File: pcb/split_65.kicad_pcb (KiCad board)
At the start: 2 copper layers, 373.9 x 95.3 mm, 312 parts, among them J1 PJ-3200B-4A, J10 AVR-ISP-6, J11 Breakaway_Tabs, J12 Breakaway_Tabs, J13 Breakaway_Tabs, J14 Breakaway_Tabs, J15 Breakaway_Tabs, J16 Breakaway_Tabs, J2 AVR-ISP-6, J3 Breakaway_Tabs, J4 Breakaway_Tabs, J5 Breakaway_Tabs, J6 Breakaway_Tabs, J7 Breakaway_Tabs, J8 Breakaway_Tabs, J9 PJ-3200B-4A, Q1 2N7002, Q2 2N7002, SW1 SW_Push, SW2 SW_Push, U1 ATmega32U4-AU, U2 PRTR5V0U2X, U3 ATmega32U4-AU, U4 PRTR5V0U2X, Y1 16MHz, Y2 16MHz

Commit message: laid out diodes and resistors
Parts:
- removed MH1, MH2: HOLE, MountingHole:MountingHole_5mm
- C1, C10, C11, C12, C13, C14, C2, C3, C4, C5, C6, C7, C8, C9, D1, D10, D11, D12, D13, D14, D15, D16, D17, D18, D19, D2, D20, D21, D22, D23, D24, D25, D26, D27, D28, D29, D3, D30, D31, D32, D33, D34, D35, D36, D37, D38, D39, D4, D40, D41, D42, D43, D44, D45, D46, D47, D48, D49, D5, D50, D51, D52, D53, D54, D55, D56, D57, D58, D59, D6, D60, D61, D62, D63, D64, D65, D66, D67, D68, D69, D7, D70, D71, D72, D73, D74, D75, D76, D77, D78, D79, D8, D80, D81, D82, D9, F1, F2, FID1, FID2, FID3, FID4, FID5, FID6, J10, J11, J12, J13, J14, J15, J16, J2, J3, J4, J5, J6, J7, J8, Q1, Q2, R1, R10, R11, R12, R13, R14, R15, R16, R17, R18, R19, R2, R20, R21, R22, R23, R24, R25, R26, R27, R28, R29, R3, R30, R31, R32, R33, R34, R35, R36, R37, R38, R39, R4, R40, R41, R42, R43, R44, R45, R46, R47, R48, R49, R5, R50, R51, R52, R53, R54, R55, R56, R57, R58, R59, R6, R60, R61, R62, R63, R64, R65, R66, R67, R68, R69, R7, R70, R71, R72, R73, R74, R75, R76, R77, R78, R79, R8, R80, R81, R82, R83, R84, R85, R86, R87, R88, R89, R9, R90, R91, R92, R93, R94, R95, R96, SW1, SW2, U1, U2, U3, U4, Y1, Y2: moved to B.Cu
- moved D8 336.0 mm to (35.7, 81.0), turned to 90 degrees
- moved D22 329.4 mm to (35.7, 119.1), turned to 90 degrees
- moved R17 323.3 mm to (35.7, 104.8), turned to 270 degrees
- moved R11 315.6 mm to (64.3, 85.7), turned to 270 degrees
- moved D9 313.6 mm to (64.4, 81.0), turned to 90 degrees
- moved R2 311.9 mm to (78.6, 66.7), turned to 270 degrees
- moved D46 311.2 mm to (381.0, 61.9), turned to 90 degrees
- moved R32 302.1 mm to (35.7, 142.9), turned to 270 degrees
- moved R88 297.9 mm to (60.3, 190.0), turned to 180 degrees
- moved Q1 297.7 mm to (60.4, 166.1), turned to 180 degrees
- moved Q2 297.7 mm to (60.4, 169.7), turned to 180 degrees
- moved R44 296.9 mm to (60.8, 201.7), turned to 180 degrees
- moved J9 294.0 mm to (264.3, 39.0), turned to 270 degrees
- moved D10 290.9 mm to (88.1, 81.0), turned to 90 degrees
- moved R91 290.1 mm to (64.2, 202.9), turned to 180 degrees
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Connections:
- MX33 pad 1: COL2 -> COL3
- MX33 pad 2: Net-(D31-Pad2) -> Net-(D32-Pad2)
- MX34 pad 4: Net-(MX33-Pad4) -> Net-(MX34-Pad4)
- MX35 pad 4: Net-(MX35-Pad4) -> Net-(MX33-Pad4)
- R34 pad 2: Net-(MX33-Pad4) -> Net-(MX34-Pad4)
- R35 pad 2: Net-(MX35-Pad4) -> Net-(MX33-Pad4)
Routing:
- net LEDGND: track 0.00 -> 455.2 mm
- net +5V: track 0.00 -> 136.0 mm
- net ROW2: track 0.00 -> 124.7 mm
- net ROW1: track 0.00 -> 119.9 mm
- net ROW4: track 0.00 -> 115.5 mm
- net ROW0: track 0.00 -> 105.7 mm
- net COL5: track 0.00 -> 69.7 mm
- net COL6: track 0.00 -> 69.6 mm
- net Net-(MX33-Pad4): track 0.00 -> 15.4 mm
- net Net-(MX31-Pad4): track 0.00 -> 9.77 mm
- net Net-(MX7-Pad4): track 0.00 -> 9.76 mm
- net Net-(MX14-Pad4): track 0.00 -> 9.76 mm
- net Net-(MX36-Pad4): track 0.00 -> 9.62 mm
- net Net-(MX12-Pad4): track 0.00 -> 7.16 mm
- net Net-(MX2-Pad4): track 0.00 -> 7.14 mm
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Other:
- board outline removed

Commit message: did edge cuts
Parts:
- J1, J9, USB1, USB2: moved to B.Cu
- moved D37 256.3 mm to (63.1, 75.6), turned to 90 degrees
- moved R42 209.6 mm to (60.7, 58.3), turned to 90 degrees
- moved R45 188.9 mm to (57.7, 56.9), turned to 270 degrees
- moved R41 172.0 mm to (63.1, 58.3), turned to 90 degrees
- moved U2 171.4 mm to (61.9, 54.2), turned to 270 degrees
- moved R44 145.9 mm to (68.1, 56.0)
- moved F1 144.2 mm to (63.1, 71.1), turned to 90 degrees
- moved D1 14.3 mm to (45.2, 61.9)
- moved R1 14.3 mm to (45.2, 66.7)
- moved J1 4.17 mm to (138.1, 44.6)
- moved USB1 2.38 mm to (61.9, 42.9), turned to 0 degrees
- turned U1 to 270 degrees
- turned USB2 to 0 degrees
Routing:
- net +5V: track 136.0 -> 332.0 mm
- net COL4: track 0.00 -> 93.0 mm
- net LEDGND: track 455.2 -> 533.5 mm
- net COL3: track 0.00 -> 69.7 mm
- net ROW3: track 0.00 -> 65.6 mm
- net GND: track 0.00 -> 62.4 mm
- net COL0: track 0.00 -> 59.5 mm
- net ROW0: track 105.7 -> 119.9 mm
- net Net-(MX16-Pad4): track 0.00 -> 12.0 mm
- net Net-(R41-Pad2): track 0.00 -> 11.2 mm
- net Net-(R42-Pad2): track 0.00 -> 10.6 mm
- net Net-(MX29-Pad4): track 0.00 -> 9.76 mm
- net Net-(MX22-Pad4): track 0.00 -> 9.76 mm
- net Net-(MX26-Pad4): track 0.00 -> 7.20 mm
- net Net-(MX28-Pad4): track 0.00 -> 7.16 mm
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- added copper zone on B.Cu, net GND
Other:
- board outline added: 158.4 x 105.4 mm

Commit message: edge cuts, route usb
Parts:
- moved R9 243.1 mm to (139.9, 60.5), turned to 90 degrees
- moved C7 205.8 mm to (57.2, 116.7)
- moved C5 201.0 mm to (45.2, 131.0)
- moved C4 199.9 mm to (40.5, 131.0)
- moved C6 197.6 mm to (57.2, 122.6)
- moved R8 146.1 mm to (136.3, 60.5), turned to 90 degrees
- moved R24 125.4 mm to (48.8, 108.3)
- moved Y1 80.0 mm to (58.3, 127.4)
- moved D5 14.3 mm to (121.4, 61.9)
- moved R5 14.3 mm to (121.4, 66.7)
- moved D37 13.8 mm to (50.1, 70.9), turned to 0 degrees
- moved F1 7.95 mm to (55.2, 70.9), turned to 0 degrees
- moved J9 5.62 mm to (264.3, 44.6)
- moved USB2 2.38 mm to (340.5, 42.9)
- moved R44 1.44 mm to (66.7, 56.0), turned to 0 degrees
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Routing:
- net GND: track 62.4 -> 149.2 mm
- net D+: track 0.00 -> 70.2 mm
- net D-: track 0.00 -> 70.2 mm
- net ROW0: track 119.9 -> 80.3 mm, vias 0 -> 2
- net LEDGND: track 533.5 -> 494.5 mm, vias 0 -> 6
- net +5V: track 332.0 -> 369.3 mm
- net VCC: track 0.00 -> 34.7 mm, vias 0 -> 2
- net Net-(R44-Pad1): track 0.00 -> 10.0 mm, vias 0 -> 2
- net Net-(MX5-Pad4): track 7.11 -> 0.00 mm
- net Net-(R45-Pad1): track 0.00 -> 6.26 mm, vias 0 -> 2
- net VBUS: track 0.00 -> 1.96 mm
- net ROW2: track 124.7 -> 125.1 mm, vias 0 -> 2
- net ROW1: track 119.9 -> 120.3 mm, vias 0 -> 2
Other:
- board size 158.4 x 105.4 mm -> 375 x 105.4 mm

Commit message: add switch, edit models
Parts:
- removed D77, D78: SOD-123, Diode_SMD:D_SOD-123
- removed D79, D80, D81: LED_3mm, locallib:LED_D3.0mm
- removed D82: Schottky, Diode_SMD:D_SOD-123
- removed R91: 1k, Resistor_SMD:R_0805_2012Metric
- removed R92, R93: 22, Resistor_SMD:R_0805_2012Metric
- removed R94: 10k, Resistor_SMD:R_0805_2012Metric
- removed R95, R96: 5.1k, Resistor_SMD:R_0805_2012Metric
- added D0: SOD-123, Diode_SMD:D_SOD-123, B.Cu at (35.7, 61.9)
- added MX0: MXOnly-1U, MX_Alps_Hybrid:MXOnly-1U, F.Cu at (28.6, 61.9)
- added R0: 470, Resistor_SMD:R_0805_2012Metric, B.Cu at (35.7, 66.7)
- D34: value LED_3mm -> Schottky; footprint locallib:LED_D3.0mm -> Diode_SMD:D_SOD-123
- D35, D36: value LED_3mm -> SOD-123; footprint locallib:LED_D3.0mm -> Diode_SMD:D_SOD-123
- D37: value Schottky -> SOD-123
- D76: value SOD-123 -> Schottky
- MX33: footprint MX_Alps_Hybrid:MXOnly-1.5U -> MX_Alps_Hybrid:MXOnly-1.25U
- MX34: footprint MX_Alps_Hybrid:MXOnly-1.25U -> MX_Alps_Hybrid:MXOnly-1.5U
- R38, R39: value 1k -> 22
- R40, R88: value 1k -> 10k
- R41, R42: value 22 -> 5.1k
- R43, R72: value 10k -> 470
- R44, R45: value 5.1k -> 470
- R69: value 470 -> 10k
- R85: value 470 -> 1k
- R86, R87: value 470 -> 22
- R89, R90: value 1k -> 5.1k
- moved D39 14.3 mm to (247.7, 61.9)
- moved R47 14.3 mm to (247.7, 66.7)
- moved R51 14.3 mm to (323.9, 66.7)
- moved D43 14.3 mm to (323.9, 61.9)
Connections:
- D34 pad 1: GND -> +5V
- D34 pad 2: Net-(D34-Pad2) -> VBUS
- D35 pad 1: GND -> ROW0-R
- D36 pad 1: GND -> ROW0-R
- D37 pad 1: +5V -> ROW0-R
- D37 pad 2: VBUS -> Net-(D37-Pad2)
- D44 pad 1: ROW0-R -> ROW1-R
- D45 pad 1: ROW0-R -> ROW1-R
- D46 pad 1: ROW0-R -> ROW1-R
- D53 pad 1: ROW1-R -> ROW2-R
- D54 pad 1: ROW1-R -> ROW2-R
- D55 pad 1: ROW1-R -> ROW2-R
- D61 pad 1: ROW2-R -> ROW3-R
- D62 pad 1: ROW2-R -> ROW3-R
- D63 pad 1: ROW2-R -> ROW3-R
- D69 pad 1: ROW3-R -> ROW4-R
- D70 pad 1: ROW3-R -> ROW4-R
- D71 pad 1: ROW3-R -> ROW4-R
- D76 pad 1: ROW4-R -> +5VA
- D76 pad 2: Net-(D76-Pad2) -> VDC
- MX1 pad 1: COL0 -> COL1
- MX10 pad 1: COL2 -> COL3
- MX11 pad 1: COL3 -> COL4
- MX12 pad 1: COL4 -> COL5
- MX13 pad 1: COL5 -> COL6
- MX14 pad 1: COL6 -> COL7
- MX15 pad 1: COL0 -> Net-(MX15-Pad1)
- MX18 pad 1: COL2 -> COL3
- MX19 pad 1: COL3 -> COL4
- MX2 pad 1: COL1 -> COL2
- MX20 pad 1: COL4 -> COL5
- MX21 pad 1: COL5 -> COL6
- MX22 pad 1: COL6 -> COL7
- MX23 pad 1: COL0 -> Net-(MX15-Pad1)
- MX25 pad 1: COL2 -> COL3
- MX26 pad 1: COL3 -> COL4
- MX27 pad 1: COL4 -> COL5
- MX28 pad 1: COL5 -> COL6
- MX29 pad 1: COL6 -> COL7
- MX3 pad 1: COL2 -> COL3
- MX30 pad 1: COL0 -> Net-(MX15-Pad1)
- MX33 pad 2: Net-(D32-Pad2) -> Net-(D31-Pad2)
- MX34 pad 1: COL2 -> COL4
- MX34 pad 2: Net-(D31-Pad2) -> Net-(D32-Pad2)
- MX35 pad 1: COL3 -> COL4
- MX35 pad 4: Net-(MX33-Pad4) -> Net-(MX34-Pad4)
- MX36 pad 1: COL4 -> COL5
- MX37 pad 1: COL4 -> COL5
- MX38 pad 2: Net-(D38-Pad2) -> Net-(D35-Pad2)
- MX39 pad 2: Net-(D39-Pad2) -> Net-(D36-Pad2)
- MX4 pad 1: COL3 -> COL4
- MX40 pad 2: Net-(D40-Pad2) -> Net-(D37-Pad2)
- MX41 pad 2: Net-(D41-Pad2) -> Net-(D38-Pad2)
- MX42 pad 2: Net-(D42-Pad2) -> Net-(D39-Pad2)
- MX43 pad 2: Net-(D43-Pad2) -> Net-(D40-Pad2)
- MX44 pad 2: Net-(D44-Pad2) -> Net-(D41-Pad2)
- MX45 pad 2: Net-(D45-Pad2) -> Net-(D42-Pad2)
- MX46 pad 2: Net-(D45-Pad2) -> Net-(D42-Pad2)
- MX47 pad 2: Net-(D46-Pad2) -> Net-(D43-Pad2)
- MX48 pad 2: Net-(D47-Pad2) -> Net-(D44-Pad2)
- MX49 pad 2: Net-(D48-Pad2) -> Net-(D45-Pad2)
- MX5 pad 1: COL4 -> COL5
- MX50 pad 2: Net-(D49-Pad2) -> Net-(D46-Pad2)
- MX51 pad 2: Net-(D50-Pad2) -> Net-(D47-Pad2)
- MX52 pad 2: Net-(D51-Pad2) -> Net-(D48-Pad2)
- MX53 pad 2: Net-(D52-Pad2) -> Net-(D49-Pad2)
- MX54 pad 2: Net-(D53-Pad2) -> Net-(D50-Pad2)
- MX55 pad 2: Net-(D54-Pad2) -> Net-(D51-Pad2)
- MX56 pad 2: Net-(D55-Pad2) -> Net-(D52-Pad2)
- MX57 pad 2: Net-(D56-Pad2) -> Net-(D53-Pad2)
- MX58 pad 2: Net-(D57-Pad2) -> Net-(D54-Pad2)
- MX59 pad 2: Net-(D58-Pad2) -> Net-(D55-Pad2)
- MX6 pad 1: COL5 -> COL6
- MX60 pad 2: Net-(D59-Pad2) -> Net-(D56-Pad2)
- MX61 pad 2: Net-(D60-Pad2) -> Net-(D57-Pad2)
- MX62 pad 2: Net-(D61-Pad2) -> Net-(D58-Pad2)
- MX63 pad 2: Net-(D62-Pad2) -> Net-(D59-Pad2)
- MX64 pad 2: Net-(D63-Pad2) -> Net-(D60-Pad2)
- MX65 pad 2: Net-(D64-Pad2) -> Net-(D61-Pad2)
- MX66 pad 2: Net-(D65-Pad2) -> Net-(D62-Pad2)
- MX67 pad 2: Net-(D66-Pad2) -> Net-(D63-Pad2)
- MX68 pad 2: Net-(D67-Pad2) -> Net-(D64-Pad2)
- MX69 pad 2: Net-(D68-Pad2) -> Net-(D65-Pad2)
- MX7 pad 1: COL6 -> COL7
- MX70 pad 2: Net-(D69-Pad2) -> Net-(D66-Pad2)
- MX71 pad 2: Net-(D70-Pad2) -> Net-(D67-Pad2)
- MX72 pad 2: Net-(D71-Pad2) -> Net-(D68-Pad2)
- MX73 pad 2: Net-(D72-Pad2) -> Net-(D69-Pad2)
- MX74 pad 2: Net-(D72-Pad2) -> Net-(D69-Pad2)
- MX75 pad 2: Net-(D73-Pad2) -> Net-(D70-Pad2)
- MX76 pad 2: Net-(D74-Pad2) -> Net-(D71-Pad2)
- MX77 pad 2: Net-(D74-Pad2) -> Net-(D71-Pad2)
- MX78 pad 2: Net-(D75-Pad2) -> Net-(D72-Pad2)
- MX79 pad 2: Net-(D75-Pad2) -> Net-(D72-Pad2)
- MX8 pad 1: COL0 -> Net-(MX15-Pad1)
- MX80 pad 2: Net-(D76-Pad2) -> Net-(D73-Pad2)
- MX81 pad 2: Net-(D77-Pad2) -> Net-(D74-Pad2)
- MX82 pad 2: Net-(D78-Pad2) -> Net-(D75-Pad2)
- R34 pad 2: Net-(MX34-Pad4) -> Net-(MX33-Pad4)
- R35 pad 2: Net-(MX33-Pad4) -> Net-(MX34-Pad4)
- R38 pad 1: Net-(D34-Pad2) -> D+
- R38 pad 2: LEDIND-1 -> Net-(R38-Pad2)
- R39 pad 1: Net-(D35-Pad2) -> D-
- R39 pad 2: LEDIND-2 -> Net-(R39-Pad2)
- R40 pad 1: Net-(D36-Pad2) -> +5V
- R40 pad 2: LEDIND-3 -> HDETECT
- R41 pad 1: D+ -> Net-(R41-Pad1)
- R41 pad 2: Net-(R41-Pad2) -> GND
- R42 pad 1: D- -> Net-(R42-Pad1)
- R42 pad 2: Net-(R42-Pad2) -> GND
- R43 pad 1: +5V -> LEDGND-R
- R43 pad 2: HDETECT -> Net-(MX38-Pad4)
- R44 pad 1: Net-(R44-Pad1) -> LEDGND-R
- R44 pad 2: GND -> Net-(MX39-Pad4)
- R45 pad 1: Net-(R45-Pad1) -> LEDGND-R
- R45 pad 2: GND -> Net-(MX40-Pad4)
- R46 pad 2: Net-(MX38-Pad4) -> Net-(MX41-Pad4)
- R47 pad 2: Net-(MX39-Pad4) -> Net-(MX42-Pad4)
- R48 pad 2: Net-(MX40-Pad4) -> Net-(MX43-Pad4)
- R49 pad 2: Net-(MX41-Pad4) -> Net-(MX44-Pad4)
- R50 pad 1: LEDGND-R -> Net-(MX45-Pad4)
- R50 pad 2: Net-(MX42-Pad4) -> LEDGND-R
- R51 pad 1: LEDGND-R -> Net-(MX47-Pad4)
- R51 pad 2: Net-(MX43-Pad4) -> LEDGND-R
- R52 pad 2: Net-(MX44-Pad4) -> Net-(MX48-Pad4)
- R53 pad 1: Net-(MX45-Pad4) -> LEDGND-R
- R53 pad 2: LEDGND-R -> Net-(MX49-Pad4)
- R54 pad 1: Net-(MX47-Pad4) -> LEDGND-R
- R54 pad 2: LEDGND-R -> Net-(MX50-Pad4)
- R55 pad 2: Net-(MX48-Pad4) -> Net-(MX51-Pad4)
- R56 pad 2: Net-(MX49-Pad4) -> Net-(MX52-Pad4)
- R57 pad 2: Net-(MX50-Pad4) -> Net-(MX53-Pad4)
- R58 pad 2: Net-(MX51-Pad4) -> Net-(MX54-Pad4)
- R59 pad 2: Net-(MX52-Pad4) -> Net-(MX55-Pad4)
- R60 pad 2: Net-(MX53-Pad4) -> Net-(MX56-Pad4)
- R61 pad 2: Net-(MX54-Pad4) -> Net-(MX57-Pad4)
- R62 pad 2: Net-(MX55-Pad4) -> Net-(MX58-Pad4)
- R63 pad 2: Net-(MX56-Pad4) -> Net-(MX59-Pad4)
- R64 pad 2: Net-(MX57-Pad4) -> Net-(MX60-Pad4)
- R65 pad 2: Net-(MX58-Pad4) -> Net-(MX61-Pad4)
- R66 pad 2: Net-(MX59-Pad4) -> Net-(MX62-Pad4)
- R67 pad 2: Net-(MX60-Pad4) -> Net-(MX63-Pad4)
- R68 pad 2: Net-(MX61-Pad4) -> Net-(MX64-Pad4)
- R69 pad 1: LEDGND-R -> GNDA
- R69 pad 2: Net-(MX62-Pad4) -> Net-(R69-Pad2)
- R70 pad 2: Net-(MX63-Pad4) -> Net-(MX65-Pad4)
- R71 pad 2: Net-(MX64-Pad4) -> Net-(MX66-Pad4)
- R72 pad 1: GNDA -> LEDGND-R
- R72 pad 2: Net-(R72-Pad2) -> Net-(MX67-Pad4)
- R73 pad 2: Net-(MX65-Pad4) -> Net-(MX68-Pad4)
- R74 pad 2: Net-(MX66-Pad4) -> Net-(MX69-Pad4)
- R75 pad 2: Net-(MX67-Pad4) -> Net-(MX70-Pad4)
- R76 pad 2: Net-(MX68-Pad4) -> Net-(MX71-Pad4)
- R77 pad 2: Net-(MX69-Pad4) -> Net-(MX72-Pad4)
- R78 pad 2: Net-(MX70-Pad4) -> Net-(MX73-Pad4)
- R79 pad 2: Net-(MX71-Pad4) -> Net-(MX75-Pad4)
- R80 pad 2: Net-(MX72-Pad4) -> Net-(MX76-Pad4)
- R81 pad 2: Net-(MX73-Pad4) -> Net-(MX78-Pad4)
- R82 pad 2: Net-(MX75-Pad4) -> Net-(MX80-Pad4)
- R83 pad 2: Net-(MX76-Pad4) -> Net-(MX81-Pad4)
- R84 pad 2: Net-(MX78-Pad4) -> Net-(MX82-Pad4)
- R85 pad 1: LEDGND-R -> Net-(Q2-Pad1)
- R85 pad 2: Net-(MX80-Pad4) -> LEDPWM-R
- R86 pad 1: LEDGND-R -> D+-R
- R86 pad 2: Net-(MX81-Pad4) -> Net-(R86-Pad2)
- R87 pad 1: LEDGND-R -> D--R
- R87 pad 2: Net-(MX82-Pad4) -> Net-(R87-Pad2)
- R88 pad 1: Net-(Q2-Pad1) -> GNDA
- R88 pad 2: LEDPWM-R -> HDETECT-R
- R89 pad 1: Net-(D79-Pad2) -> Net-(R89-Pad1)
- R89 pad 2: LEDIND-1-R -> GNDA
- R90 pad 1: Net-(D80-Pad2) -> Net-(R90-Pad1)
- R90 pad 2: LEDIND-2-R -> GNDA
- U1 pad 29: LEDIND-1 -> Net-(U1-Pad29)
- U1 pad 30: LEDIND-2 -> Net-(U1-Pad30)
- U1 pad 31: LEDIND-3 -> Net-(U1-Pad31)
- U2 pad 2: Net-(R41-Pad2) -> Net-(R38-Pad2)
- U2 pad 3: Net-(R42-Pad2) -> Net-(R39-Pad2)
- U3 pad 32: LEDIND-3-R -> Net-(U3-Pad32)
- U3 pad 33: Net-(R72-Pad2) -> Net-(R69-Pad2)
- U3 pad 36: LEDIND-2-R -> Net-(U3-Pad36)
- U3 pad 37: LEDIND-1-R -> Net-(U3-Pad37)
- U4 pad 2: Net-(R92-Pad2) -> Net-(R86-Pad2)
- U4 pad 3: Net-(R93-Pad2) -> Net-(R87-Pad2)
- USB1 pad 10: Net-(R44-Pad1) -> Net-(R41-Pad1)
- USB1 pad 4: Net-(R45-Pad1) -> Net-(R42-Pad1)
- USB1 pad 5: Net-(R42-Pad2) -> Net-(R39-Pad2)
- USB1 pad 6: Net-(R41-Pad2) -> Net-(R38-Pad2)
- USB1 pad 7: Net-(R42-Pad2) -> Net-(R39-Pad2)
- USB1 pad 8: Net-(R41-Pad2) -> Net-(R38-Pad2)
- USB2 pad 10: Net-(R95-Pad1) -> Net-(R89-Pad1)
- USB2 pad 4: Net-(R96-Pad1) -> Net-(R90-Pad1)
- USB2 pad 5: Net-(R93-Pad2) -> Net-(R87-Pad2)
- USB2 pad 6: Net-(R92-Pad2) -> Net-(R86-Pad2)
- USB2 pad 7: Net-(R93-Pad2) -> Net-(R87-Pad2)
- USB2 pad 8: Net-(R92-Pad2) -> Net-(R86-Pad2)
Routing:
- net COL3: track 69.7 -> 0.00 mm
- net COL7: track 0.00 -> 69.6 mm
- net Net-(MX15-Pad1): track 0.00 -> 59.5 mm
- net COL0: track 59.5 -> 0.00 mm
- net +5V: track 369.3 -> 332.0 mm
- net ROW0-R: track 0.00 -> 37.3 mm
- net COL5: track 69.7 -> 93.0 mm
- net COL4: track 93.0 -> 69.7 mm
- net ROW0: track 80.3 -> 90.7 mm
- net LEDGND: track 494.5 -> 504.6 mm
- net Net-(MX0-Pad4): track 0.00 -> 6.13 mm

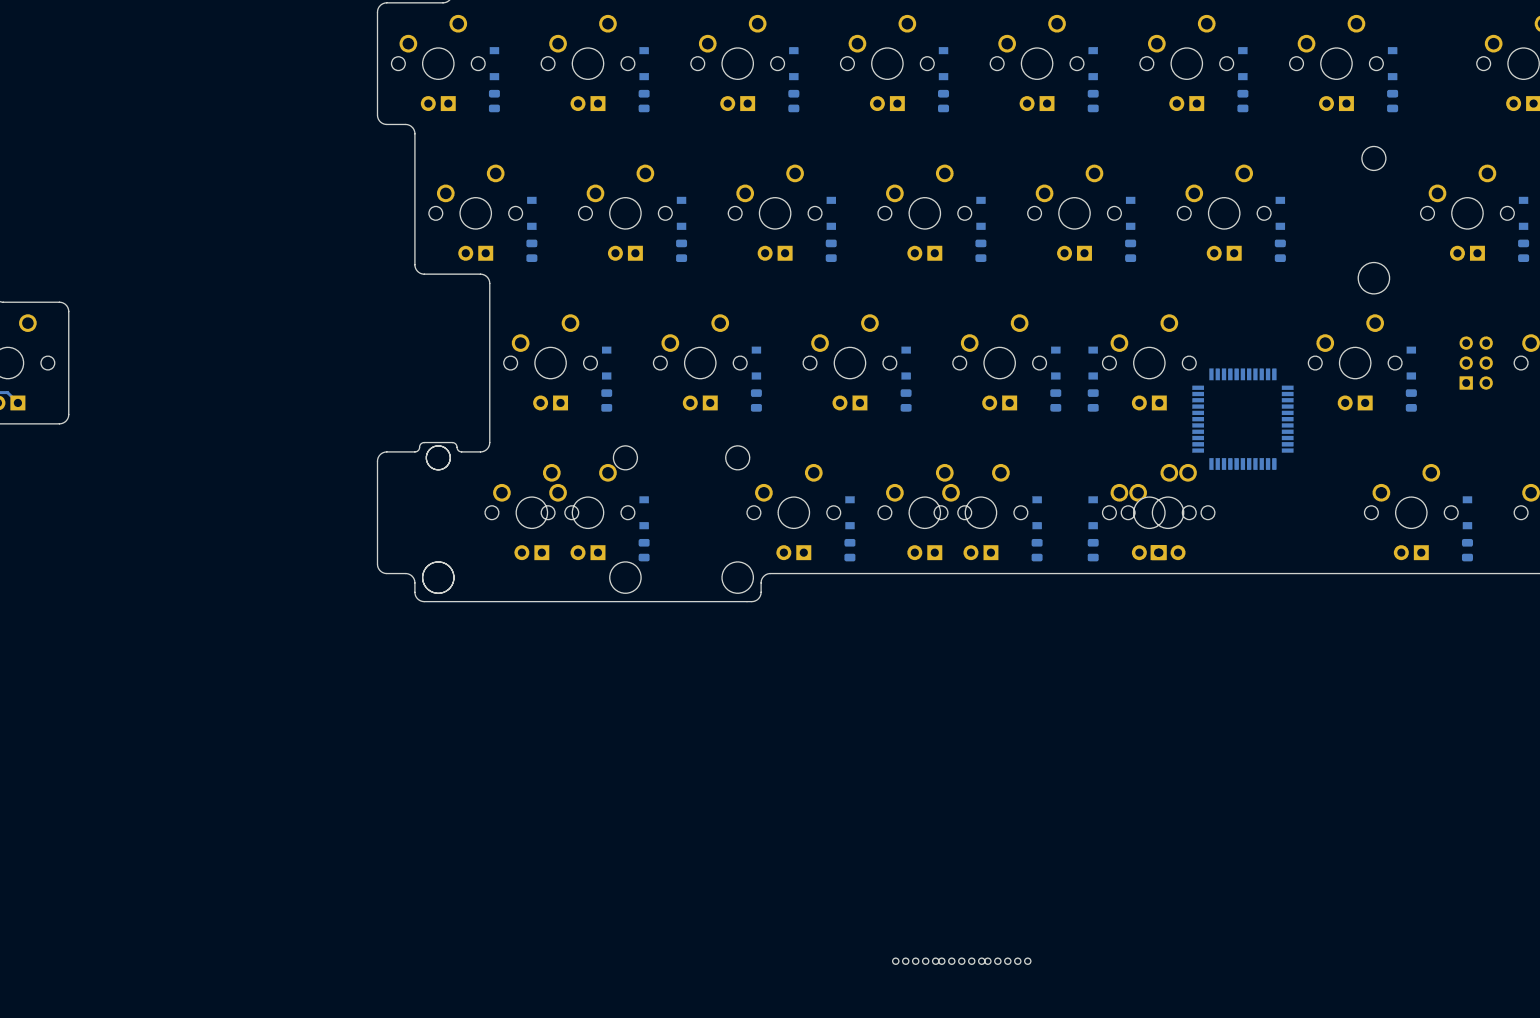
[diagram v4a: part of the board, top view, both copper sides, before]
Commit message: add resistor to rst, rgb underglow
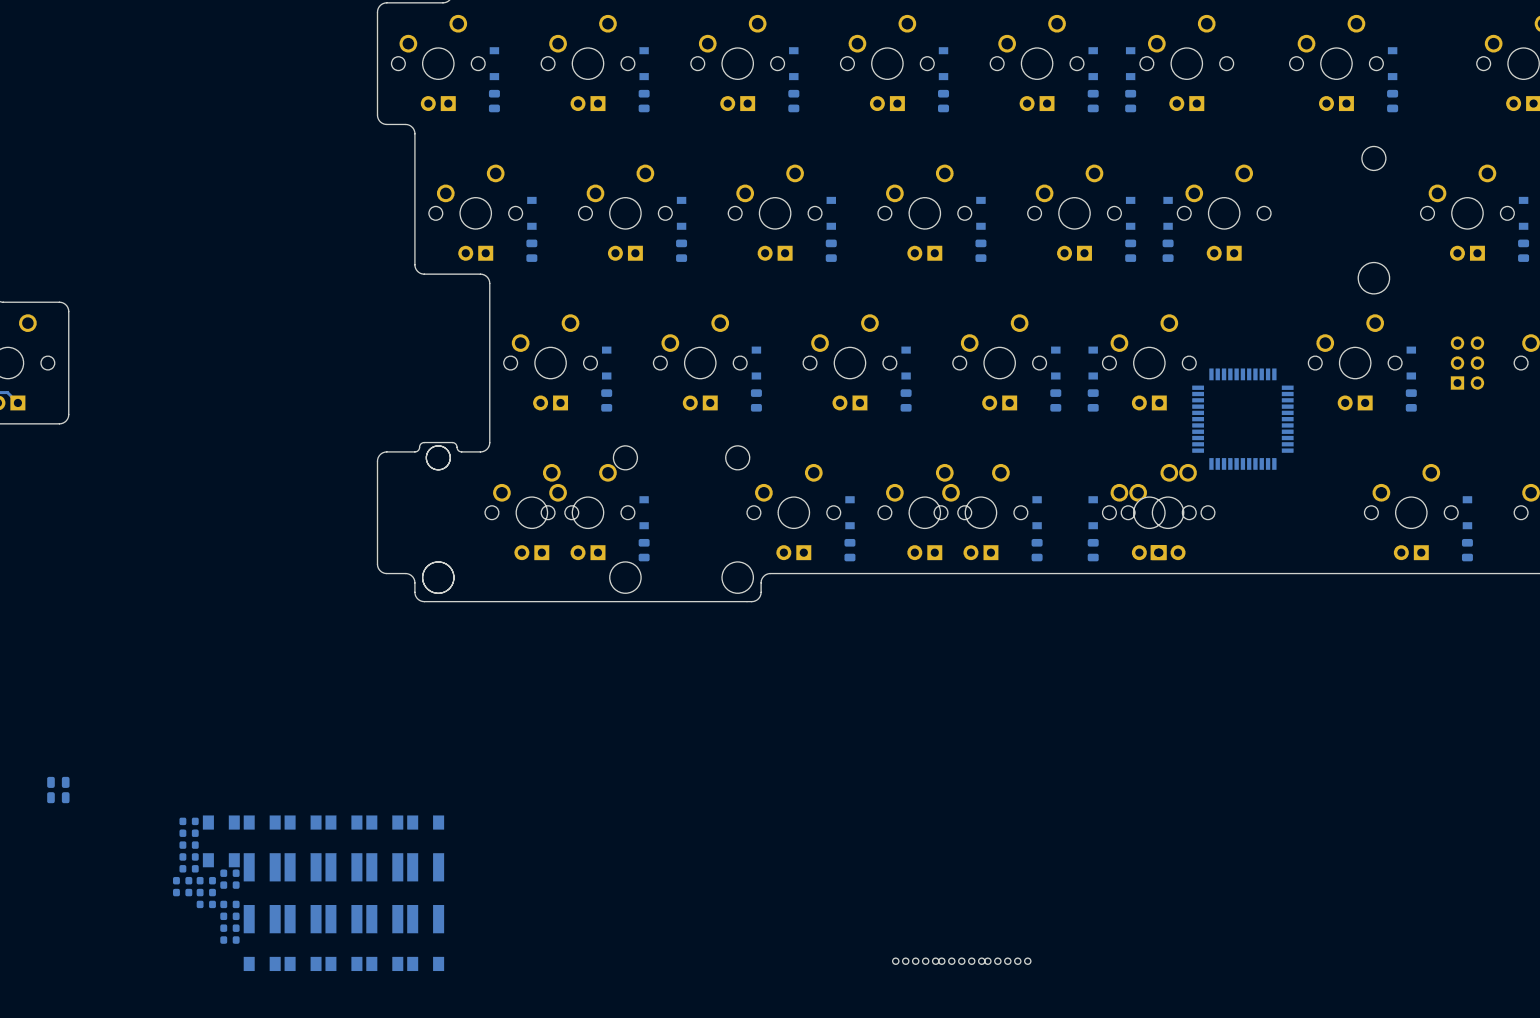
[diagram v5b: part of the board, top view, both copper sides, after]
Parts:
- added C15: 0.1uF, Capacitor_SMD:C_0603_1608Metric, B.Cu at (199.7, 192.5)
- added C16: 0.1uF, Capacitor_SMD:C_0603_1608Metric, B.Cu at (194.5, 177.4)
- added C17: 0.1uF, Capacitor_SMD:C_0603_1608Metric, B.Cu at (199.7, 184.0)
- added C18: 0.1uF, Capacitor_SMD:C_0603_1608Metric, B.Cu at (199.7, 185.5)
- added C19: 0.1uF, Capacitor_SMD:C_0603_1608Metric, B.Cu at (194.5, 178.9)
- added C20: 0.1uF, Capacitor_SMD:C_0603_1608Metric, B.Cu at (194.5, 180.4)
- added C21: 0.1uF, Capacitor_SMD:C_0603_1608Metric, B.Cu at (194.5, 181.9)
- added C22: 0.1uF, Capacitor_SMD:C_0603_1608Metric, B.Cu at (194.5, 183.4)
- added C23: 0.1uF, Capacitor_SMD:C_0603_1608Metric, B.Cu at (196.7, 184.9)
- added C24: 0.1uF, Capacitor_SMD:C_0603_1608Metric, B.Cu at (193.7, 184.9)
- added C25: 0.1uF, Capacitor_SMD:C_0603_1608Metric, B.Cu at (196.7, 186.4)
- added C26: 0.1uF, Capacitor_SMD:C_0603_1608Metric, B.Cu at (199.7, 188.0)
- added C27: 0.1uF, Capacitor_SMD:C_0603_1608Metric, B.Cu at (196.7, 188.0)
- added C28: 0.1uF, Capacitor_SMD:C_0603_1608Metric, B.Cu at (199.7, 189.5)
- added C29: 0.1uF, Capacitor_SMD:C_0603_1608Metric, B.Cu at (199.7, 191.0)
- added C30: 0.1uF, Capacitor_SMD:C_0603_1608Metric, B.Cu at (193.7, 186.4)
- added LED1: WS2812B, WS2812B:WS2812B, B.Cu at (224.6, 186.5)
- added LED10: WS2812B, WS2812B:WS2812B, B.Cu at (203.8, 179.9)
- added LED11: WS2812B, WS2812B:WS2812B, B.Cu at (209.0, 186.5)
- added LED12: WS2812B, WS2812B:WS2812B, B.Cu at (203.8, 186.5)
- added LED13: WS2812B, WS2812B:WS2812B, B.Cu at (209.0, 193.1)
- added LED14: WS2812B, WS2812B:WS2812B, B.Cu at (198.6, 179.9)
- added LED15: WS2812B, WS2812B:WS2812B, B.Cu at (203.8, 193.1)
- added LED16: WS2812B, WS2812B:WS2812B, B.Cu at (224.6, 179.9)
- added LED2: WS2812B, WS2812B:WS2812B, B.Cu at (219.4, 179.9)
- added LED3: WS2812B, WS2812B:WS2812B, B.Cu at (224.6, 193.1)
- added LED4: WS2812B, WS2812B:WS2812B, B.Cu at (214.2, 179.9)
- added LED5: WS2812B, WS2812B:WS2812B, B.Cu at (219.4, 186.5)
- added LED6: WS2812B, WS2812B:WS2812B, B.Cu at (214.2, 186.5)
- added LED7: WS2812B, WS2812B:WS2812B, B.Cu at (219.4, 193.1)
- added LED8: WS2812B, WS2812B:WS2812B, B.Cu at (209.0, 179.9)
- added LED9: WS2812B, WS2812B:WS2812B, B.Cu at (214.2, 193.1)
- added R91: 10k, Resistor_SMD:R_0805_2012Metric, B.Cu at (177.9, 172.4)
- added R92: 10k, Resistor_SMD:R_0805_2012Metric, B.Cu at (177.9, 174.4)
- moved D52 14.3 mm to (314.3, 81.0)
- moved R60 14.3 mm to (314.3, 85.7)
- moved D61 14.3 mm to (319.1, 100.0)
- moved R69 14.3 mm to (319.1, 104.8)
- moved J10 1.11 mm to (357.2, 119.1)
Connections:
- MX15 pad 1: Net-(MX15-Pad1) -> COL0
- MX23 pad 1: Net-(MX15-Pad1) -> COL0
- MX30 pad 1: Net-(MX15-Pad1) -> COL0
- MX8 pad 1: Net-(MX15-Pad1) -> COL0
- SW1 pad 2: RESET -> Net-(R91-Pad1)
- SW2 pad 2: RESET-R -> Net-(R92-Pad1)
- U1 pad 13: RESET -> Net-(R91-Pad1)
- U3 pad 13: RESET-R -> Net-(R92-Pad1)
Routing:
- net Net-(MX15-Pad1): track 59.5 -> 0.00 mm
- net COL0: track 0.00 -> 59.5 mm
